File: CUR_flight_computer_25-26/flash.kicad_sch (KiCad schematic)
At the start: 16 parts, among them J6 MSD-4-A, U10 W25Q32JVSS

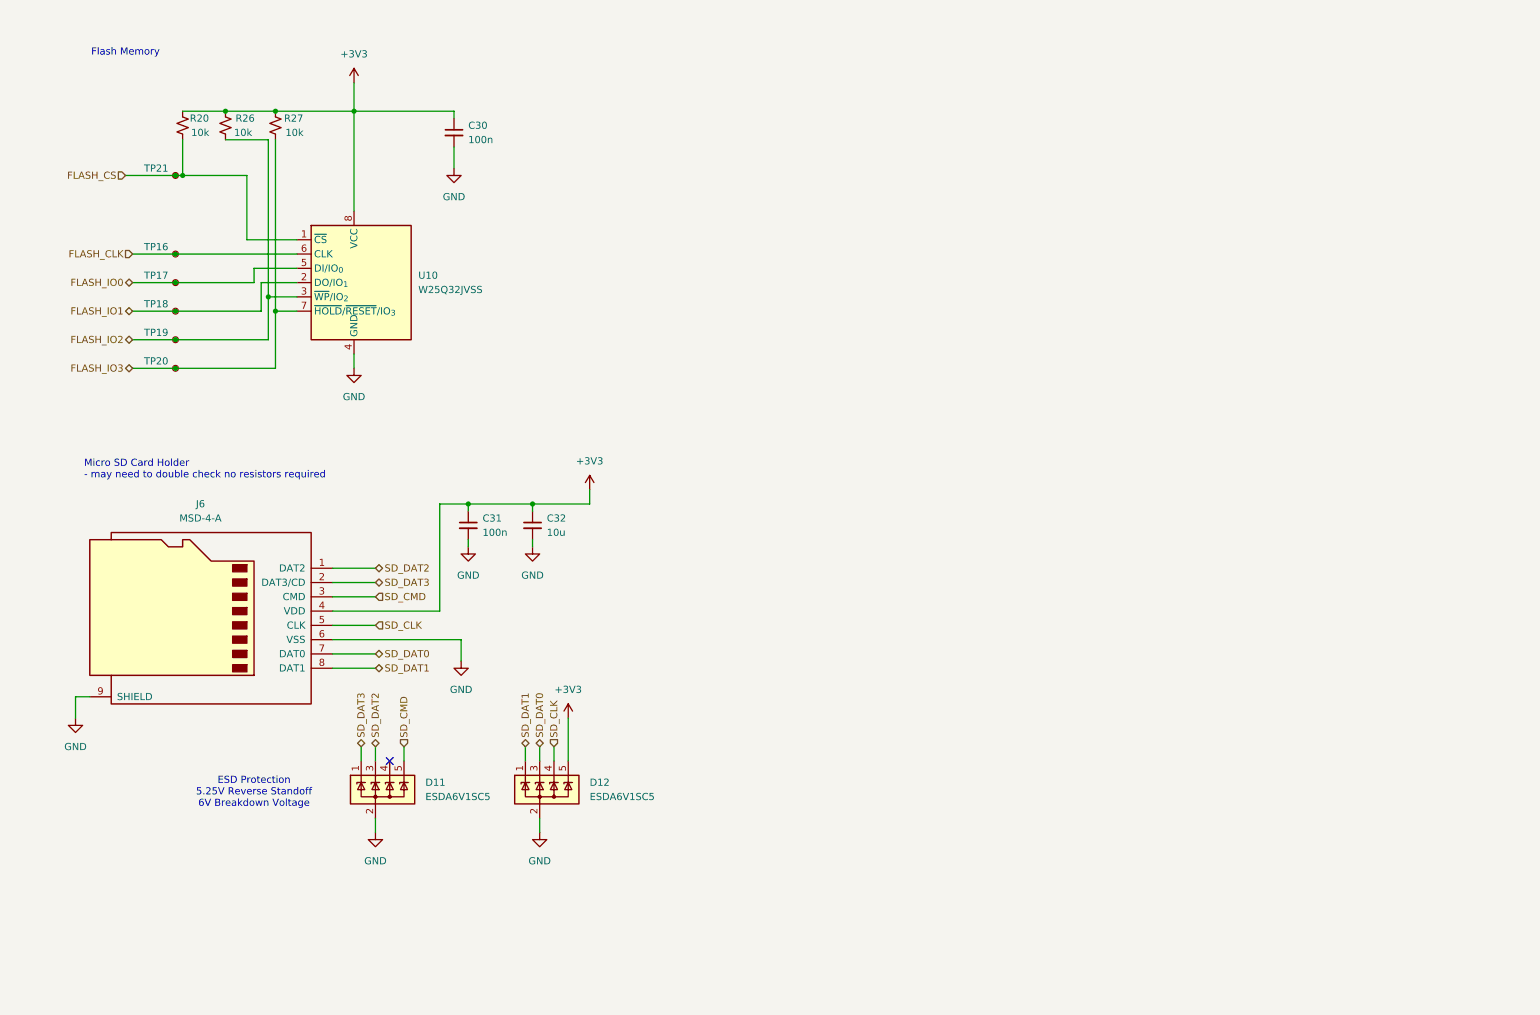
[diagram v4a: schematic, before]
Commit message: Cleaned up schematic
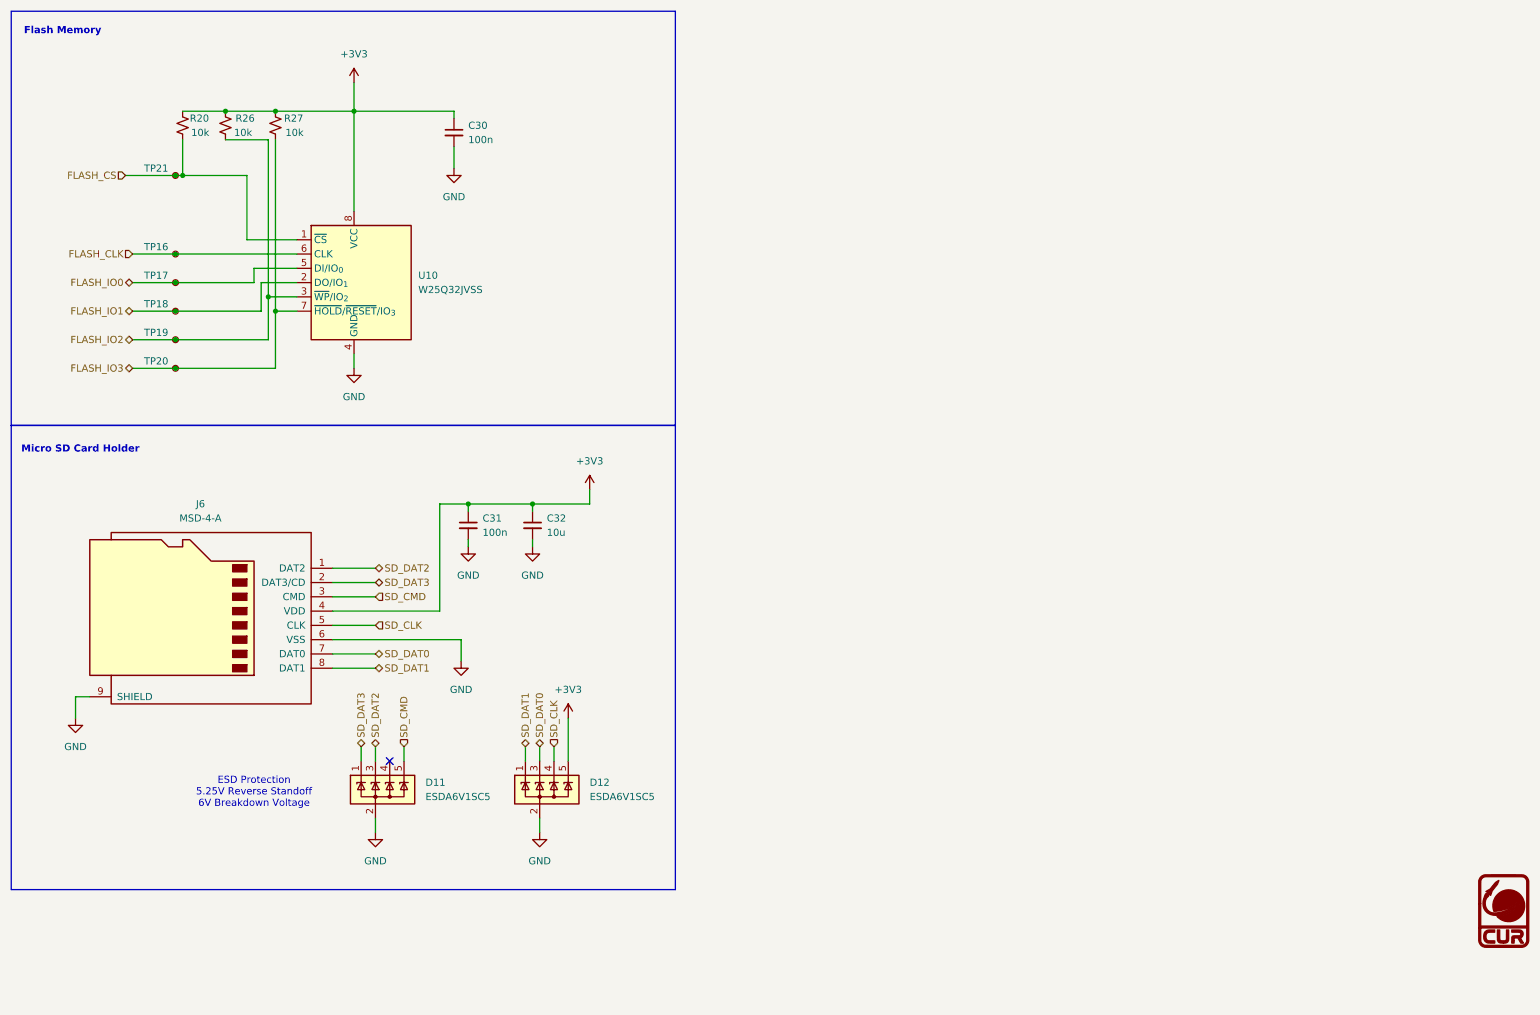
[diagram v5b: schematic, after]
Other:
- note added: "Micro SD Card Holder"
- note removed: "Micro SD Card Holder - may need to double check no resistors required"
- company: (none) -> Clarkson University Rocketry
- title: (none) -> Flight Computer
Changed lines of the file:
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@@
 	(generator_version "9.0")
 	(paper "A4")
+	(title_block
+		(title "Flight Computer")
+		(date "2026-03-18")
+		(company "Clarkson University Rocketry")
+	)
+	(rectangle
+		(start 13.97 13.97)
+		(end 132.08 87.63)
+		(stroke
+			(width 0)
+			(type default)
+		)
+		(fill
+			(type none)
+		)
+	)
+	(rectangle
+		(start 13.97 87.63)
+		(end 132.08 170.18)
+		(stroke
+			(width 0)
+			(type default)
+		)
+		(fill
+			(type none)
+		)
+	)
 	(text "ESD Protection\n5.25V Reverse Standoff\n6V Breakdown Voltage\n"
 		(exclude_from_sim no)
@@
 		)
 	)
-	(text "Micro SD Card Holder\n- may need to double check no resistors required\n"
-		(exclude_from_sim no)
-		(at 26.924 95.504 0)
+	(text "Micro SD Card Holder\n\n"
+		(exclude_from_sim no)
+		(at 15.748 92.964 0)
 		(effects
 			(font
 				(size 1.27 1.27)
+				(thickness 0.254)
+				(bold yes)
 			)
 			(justify left)
@@
 	(text "Flash Memory"
 		(exclude_from_sim no)
-		(at 34.29 21.336 0)
+		(at 23.114 17.526 0)
 		(effects
 			(font
 				(size 1.27 1.27)
+				(thickness 0.254)
+				(bold yes)
 			)
 		)
@@
 					(unit 1)
 				)
+			)
+		)
+	)
+	(symbol
+		(lib_id "CUR_Logo:LOGO")
+		(at 279.4 173.99 0)
+		(unit 1)
+		(exclude_from_sim no)
+		(in_bom yes)
+		(on_board yes)
+		(dnp no)
+		(fields_autoplaced yes)
+		(property "Reference" "#G7"
+			(at 279.4 167.002 0)
+			(effects
+				(font
+					(size 1.27 1.27)
+				)
+				(hide yes)
+			)
+		)
+		(property "Value" "LOGO"
+			(at 279.4 180.978 0)
+			(effects
+				(font
+					(size 1.27 1.27)
+				)
+				(hide yes)
+			)
+		)
+		(property "Footprint" ""
+			(at 279.4 173.99 0)
+			(effects
+				(font
+					(size 1.27 1.27)
+				)
+				(hide yes)
+			)
+		)
+		(property "Datasheet" ""
+			(at 279.4 173.99 0)
+			(effects
+				(font
+					(size 1.27 1.27)
+				)
+				(hide yes)
+			)
+		)
+		(property "Description" ""
+			(at 279.4 173.99 0)
+			(effects
+				(font
+					(size 1.27 1.27)
+				)
+				(hide yes)
+			)
+		)
+		(instances
+			(project "CUR_flight_computer_25-26"
+				(path "/bf7761cc-1b32-4d86-809c-5f027005229b/6e71e7a3-1bcd-4797-b2e4-88d14bf1f853"
+					(reference "#G7")
+					(unit 1)
+				)

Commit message: Replace SD card holder, route GPS I2C again
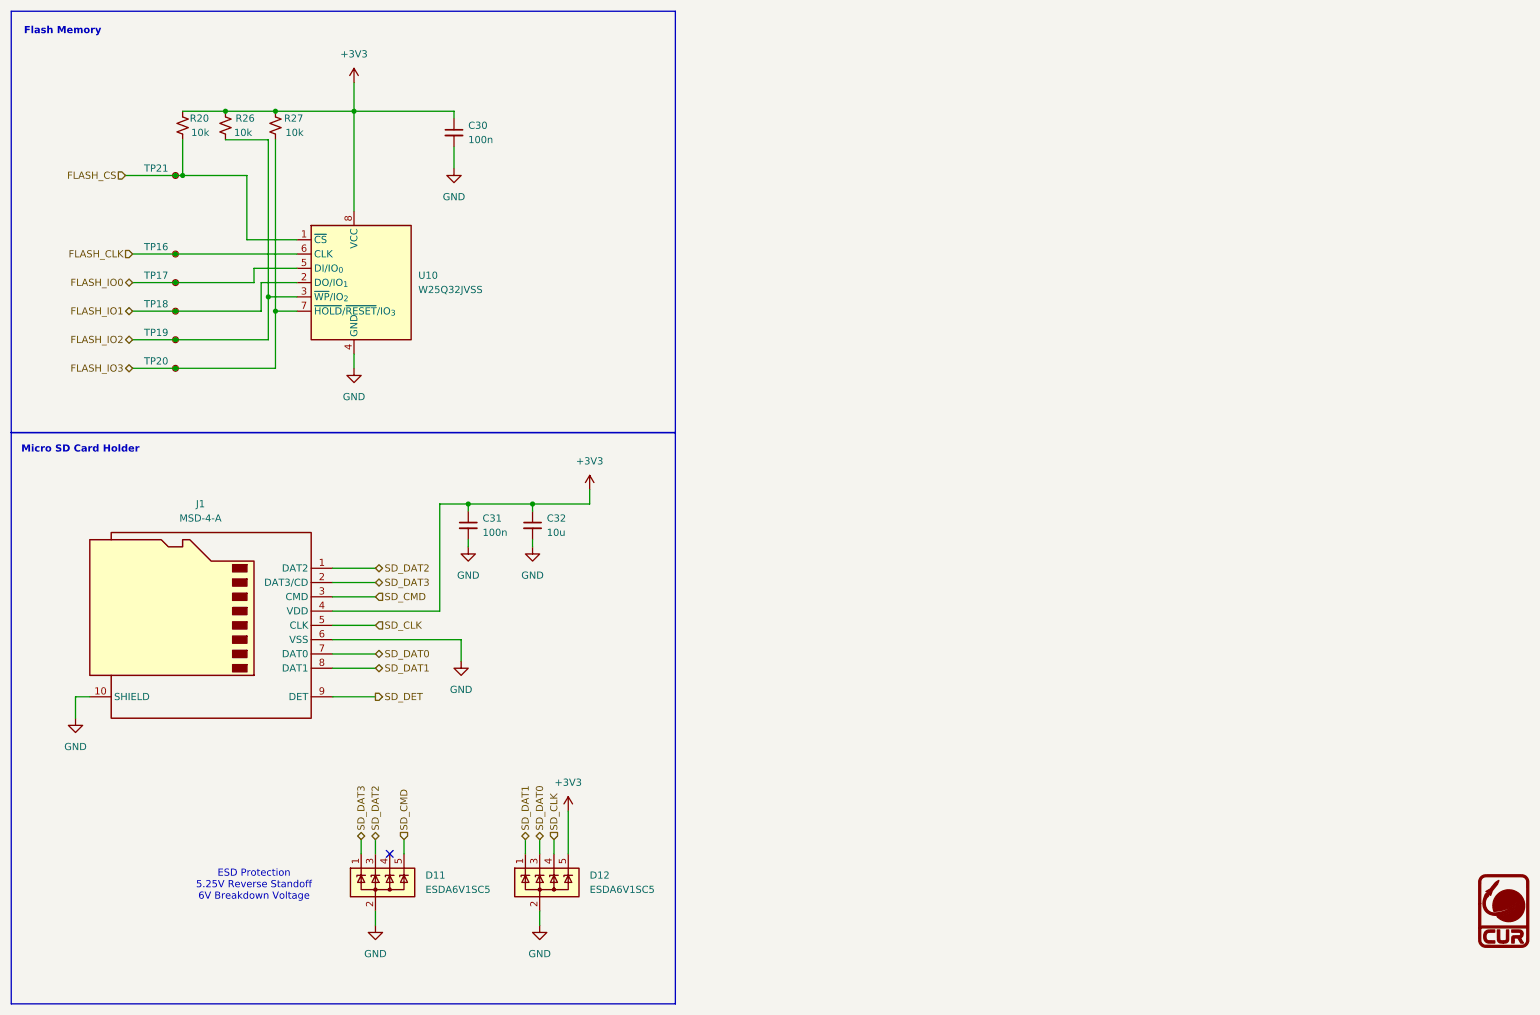
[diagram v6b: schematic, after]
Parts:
- removed J6: MSD-4-A, MSD-4-A:CUI_MSD-4-A, symbol Connector:Micro_SD_Card
- added J1: MSD-4-A, MSD-4-A:CUI_MSD-4-A, symbol Connector:Micro_SD_Card_Det1
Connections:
- net +3V3: now also J1.4 (VDD)
- net GND: now also J1.10 (SHIELD), J1.6 (VSS)
- net SD_CLK: now also J1.5 (CLK)
- net SD_CMD: now also J1.3 (CMD)
- net SD_DAT0: now also J1.7 (DAT0)
- net SD_DAT1: now also J1.8 (DAT1)
- net SD_DAT2: now also J1.1 (DAT2)
- net SD_DAT3: now also J1.2 (DAT3/CD)
- new net SD_DET: J1.9 (DET)
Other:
- moved on the sheet: D11, D12

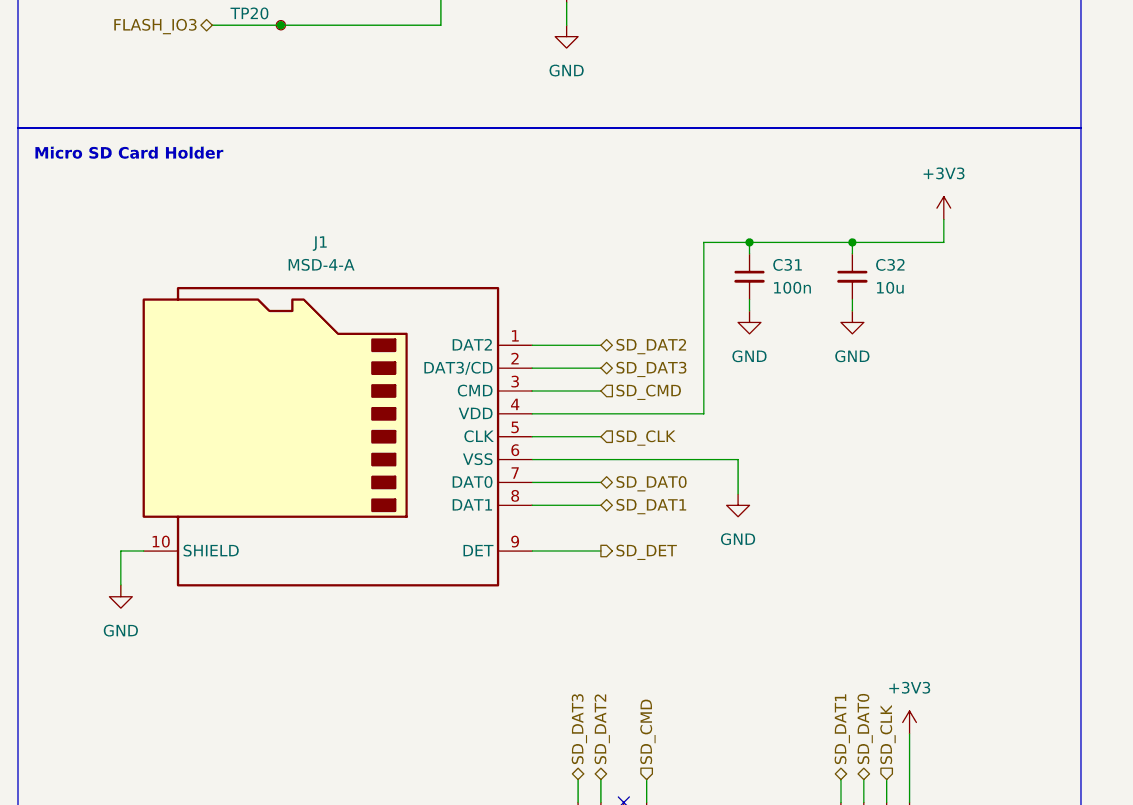
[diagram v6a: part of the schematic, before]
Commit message: added sd card detect
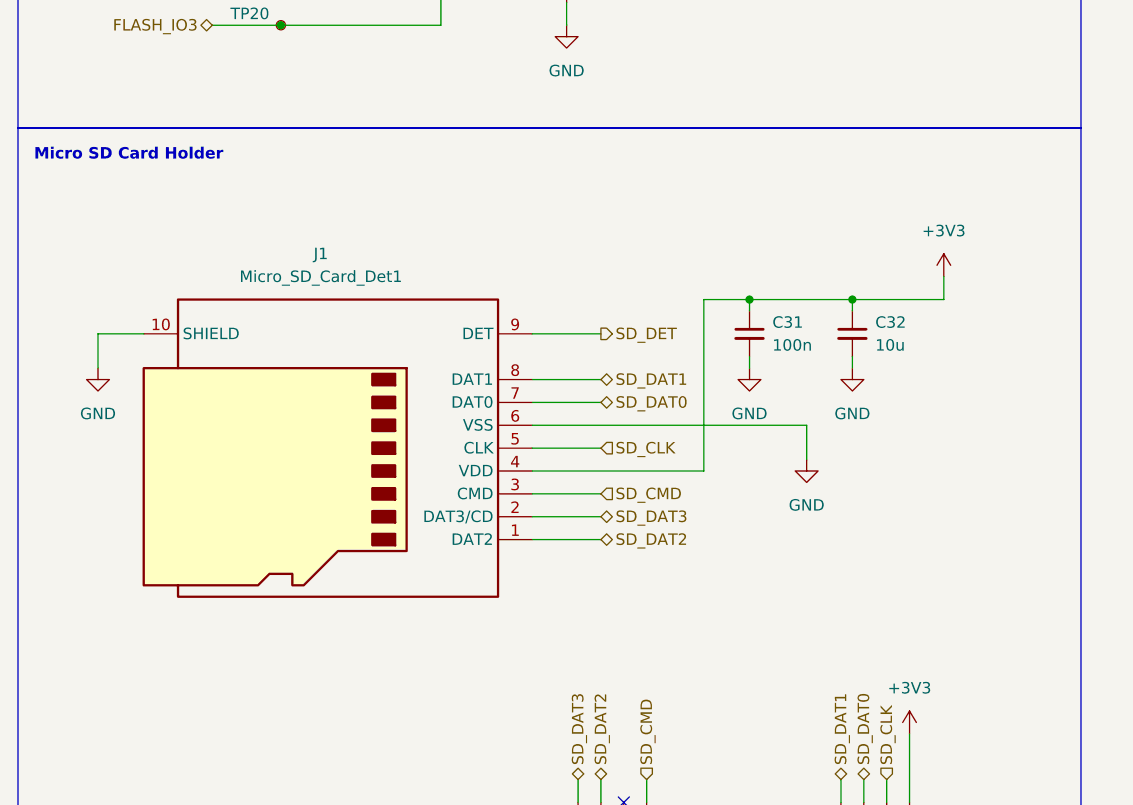
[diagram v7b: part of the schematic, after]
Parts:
- J1: value MSD-4-A -> Micro_SD_Card_Det1
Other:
- moved on the sheet: C31, C32

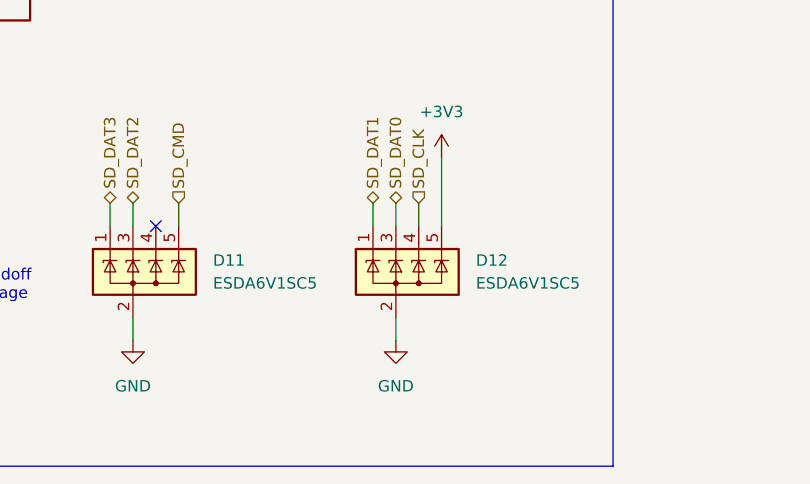
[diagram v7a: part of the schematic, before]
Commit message: BOM optimize TVS diodes on SD card to match debug
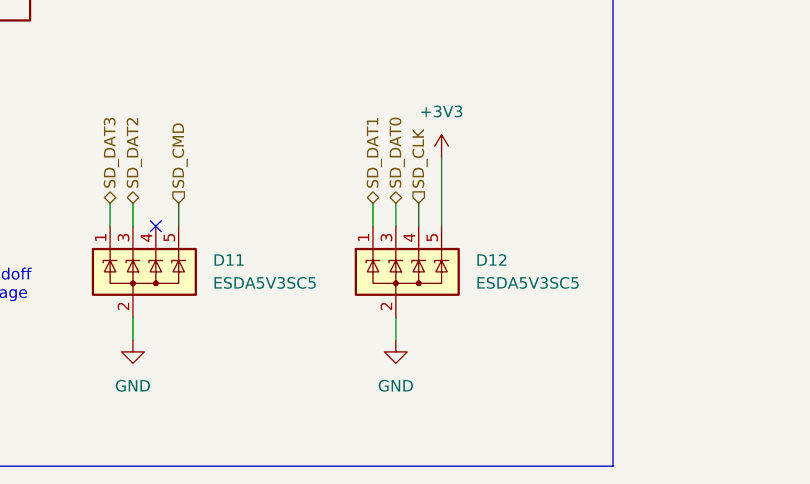
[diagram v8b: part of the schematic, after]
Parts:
- D11, D12: value ESDA6V1SC5 -> ESDA5V3SC5
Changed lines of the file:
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@@
 			)
 		)
-		(property "Value" "ESDA6V1SC5"
+		(property "Value" "ESDA5V3SC5"
 			(at 87.63 170.1799 0)
 			(effects
@@
 			)
 		)
-		(property "Value" "ESDA6V1SC5"
+		(property "Value" "ESDA5V3SC5"
 			(at 116.84 170.1799 0)
 			(effects
